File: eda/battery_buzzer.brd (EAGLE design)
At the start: 47 x 26.7 mm, 28 parts, among them Q2 IRFML8244, U1 ISL83491SOIC, U2 ATTINY1634

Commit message: Much tidying in pie.lbr
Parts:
- U2: device pie:SOIC20S -> pie:SOIC20
- moved U2 7.41 mm to (16.5, 14.0), turned to 180 degrees

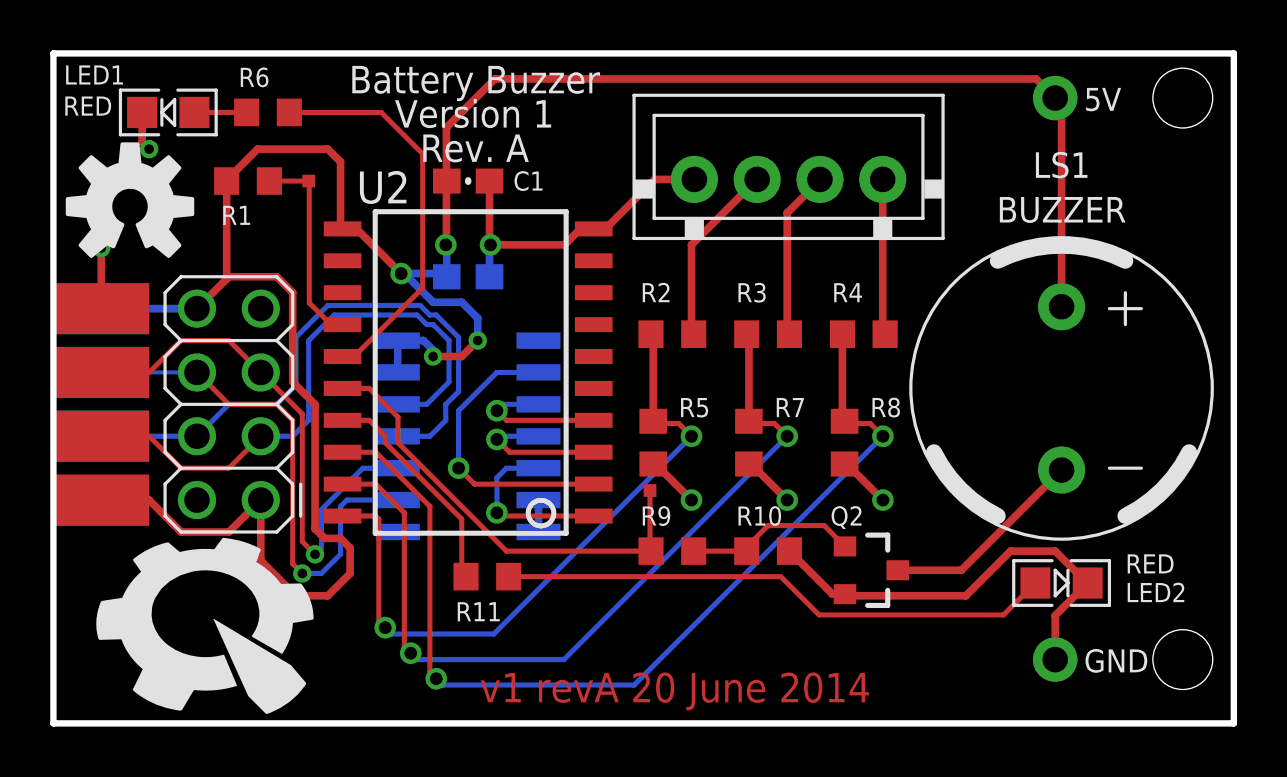
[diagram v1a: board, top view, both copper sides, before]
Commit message: Fixed ribboncable pinout
On battery_buzzer, smartsensor, smartsensor_Powered, team_flag, controller,
and grizzly_bear.
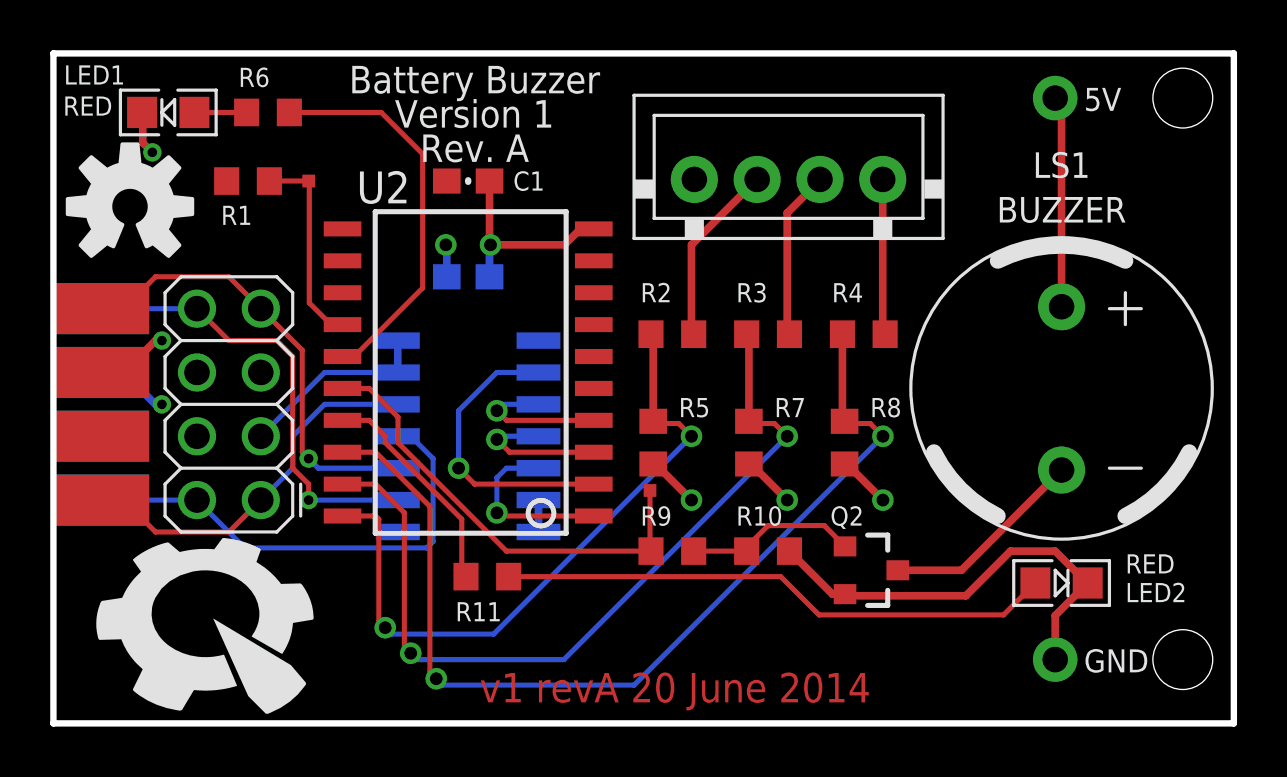
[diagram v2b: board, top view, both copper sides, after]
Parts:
- renumbered U$7 to U$14, U$8 to U$15
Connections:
- net 5V: now also U$14.3, U$14.6, U$15.3, U$15.6; no longer U$14.1, U$14.8, U$15.1, U$15.8
- net A_N: now also U$14.2, U$15.2; no longer U$14.4, U$15.4
- net A_P: now also U$14.1, U$15.1; no longer U$14.3, U$15.3
- net B_N: now also U$14.7, U$15.7; no longer U$14.5, U$15.5
- net B_P: now also U$14.8, U$15.8; no longer U$14.6, U$15.6
- net GND: now also U$14.4, U$14.5, U$15.4, U$15.5; no longer U$14.2, U$14.7, U$15.2, U$15.7
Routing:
- net 5V: track 102.0 -> 21.6 mm, vias 4 -> 2
- net A_P: track 23.2 -> 15.2 mm
- net GND: track 45.3 -> 39.2 mm
- net A_N: track 23.7 -> 19.2 mm
- net B_N: track 21.1 -> 17.9 mm
- net B_P: track 20.8 -> 17.9 mm
- added copper zone on layer 1, net 5V
- removed copper zone on layer 1, net N$8

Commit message: All jigs probe vias accessible after populating.
Also changed "VCC" signal name on jigs to "5V" to match boards.
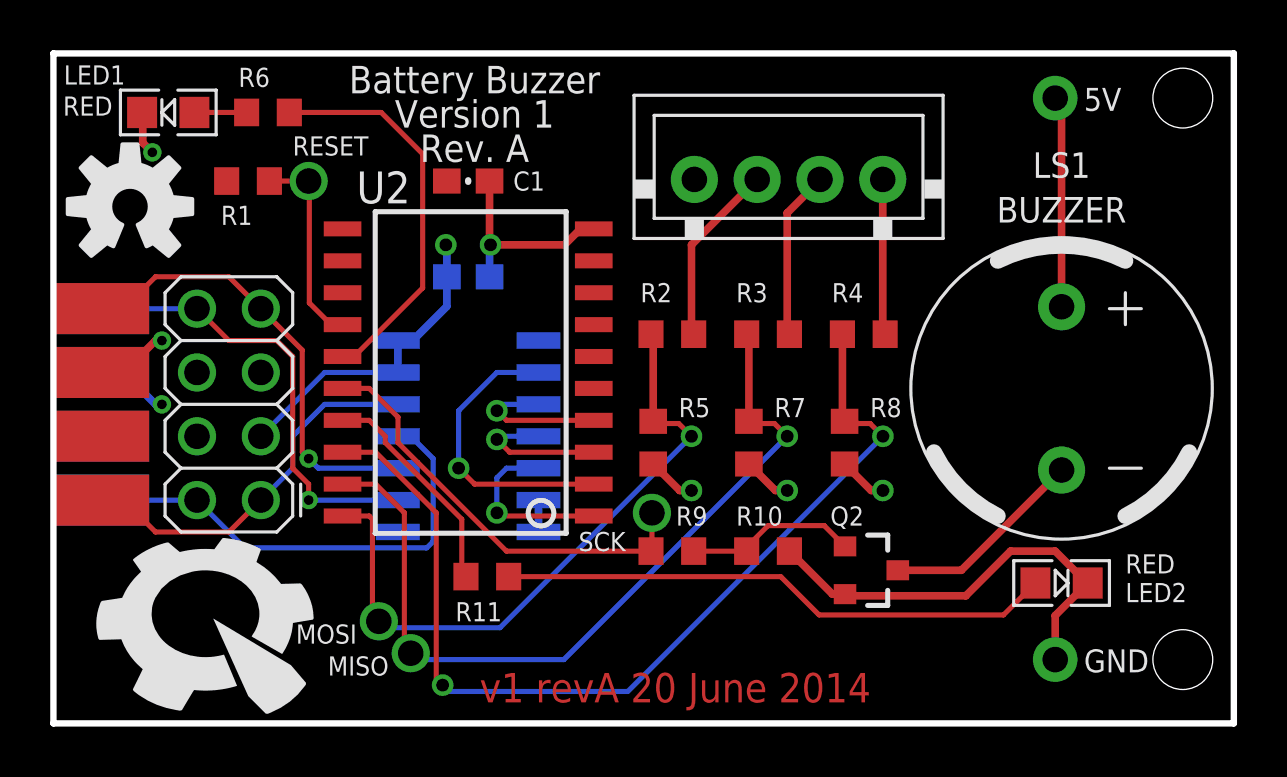
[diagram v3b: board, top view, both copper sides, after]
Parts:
- removed TP1, TP2: TEST-POINT2, pie:PAD.02X.02
- added MISO, MOSI, RESET, SCK: (no value), pie:POGO_PIN_394
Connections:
- net IO1: now also MOSI.POGO_PIN
- net IO2: now also MISO.POGO_PIN
- net IO3: now also SCK.POGO_PIN; no longer TP2.P$1
- net RESET: now also RESET.POGO_PIN; no longer TP1.P$1
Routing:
- net 5V: track 21.6 -> 25.3 mm
- net GND: track 39.2 -> 40.2 mm
- net IO3: track 18.1 -> 17.2 mm
- net IO1: track 26.9 -> 26.6 mm, vias 2 -> 1
- net IO2: vias 2 -> 1

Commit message: battery_buzzer.brd LED orientation and silkscreen fixed.
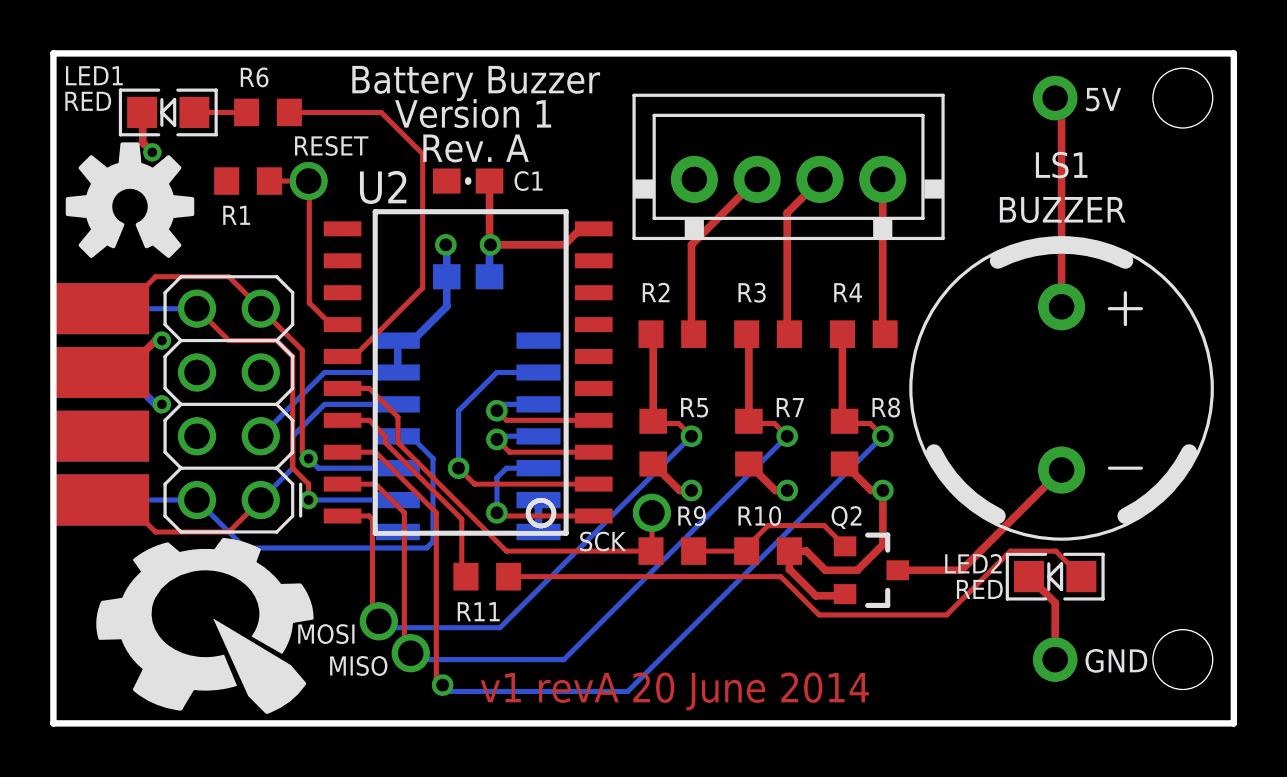
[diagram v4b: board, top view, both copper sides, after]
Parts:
- moved LED2 0.36 mm to (39.9, 5.84), turned to 180 degrees
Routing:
- net GND: track 40.2 -> 36.6 mm
- net N$7: track 22.1 -> 24.9 mm
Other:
- board text added: "10k"
- board text removed: "110k"
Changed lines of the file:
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@@
 <wire x1="0" y1="26.67" x2="0" y2="0" width="0.254" layer="20"/>
 <text x="16.9672" y="0.8382" size="1.1684" layer="1" font="vector" ratio="15">v1 revA 20 June 2014</text>
-<text x="38.354" y="1.016" size="0.762" layer="22" font="vector" ratio="20" rot="MR0">(c) Pioneers in Engineering
+<text x="38.608" y="1.27" size="0.762" layer="22" font="vector" ratio="20" rot="MR0">(c) Pioneers in Engineering
 Design by:
 Vincent Donato, Devin He, and Krystyn Neisess
@@
 Rev. A</text>
 <text x="7.366" y="23.368" size="0.762" layer="27" font="vector" ratio="20" align="top-left">130</text>
-<text x="6.6802" y="19.7104" size="0.762" layer="27" font="vector" ratio="20" align="top-left">110k</text>
+<text x="6.6802" y="19.5834" size="0.762" layer="27" font="vector" ratio="20" align="top-left">10k</text>
 </plain>
 <attributes>
@@
 <element name="LED1" library="pie" package="LED-0805" value="RED" x="4.572" y="24.3205" smashed="yes" rot="R180">
 <attribute name="PIE-INT-REF-NUM" value="LED" x="4.572" y="24.3205" size="1.778" layer="27" rot="R180" display="off"/>
-<attribute name="NAME" x="0.41275" y="25.43175" size="0.762" layer="25" font="vector" ratio="20"/>
-<attribute name="VALUE" x="0.381" y="24.1935" size="0.762" layer="25" font="vector" ratio="20"/>
+<attribute name="NAME" x="0.4064" y="25.4" size="0.762" layer="25" font="vector" ratio="20"/>
+<attribute name="VALUE" x="0.381" y="24.384" size="0.762" layer="25" font="vector" ratio="20"/>
 </element>
 <element name="U$11" library="pie" package="XH_CONNECTOR_4POS_2.5MM" value="XH_CONNECTOR_4POS" x="29.464" y="21.844" smashed="yes">
@@
 <attribute name="VALUE" x="16.002" y="2.921" size="0.762" layer="27" font="vector" ratio="20"/>
 </element>
-<element name="LED2" library="pie" package="LED-0805" value="RED" x="40.132" y="5.588" smashed="yes">
-<attribute name="PIE-INT-REF-NUM" value="LED" x="40.132" y="5.588" size="1.778" layer="27" display="off"/>
-<attribute name="NAME" x="42.672" y="4.826" size="0.762" layer="25" font="vector" ratio="20"/>
-<attribute name="VALUE" x="42.672" y="5.969" size="0.762" layer="25" font="vector" ratio="20"/>
+<element name="LED2" library="pie" package="LED-0805" value="RED" x="39.878" y="5.842" smashed="yes" rot="R180">
+<attribute name="PIE-INT-REF-NUM" value="LED" x="39.878" y="5.842" size="1.778" layer="27" rot="R180" display="off"/>
+<attribute name="NAME" x="37.846" y="6.731" size="0.762" layer="25" font="vector" ratio="20" rot="R180"/>
+<attribute name="VALUE" x="37.846" y="5.715" size="0.762" layer="25" font="vector" ratio="20" rot="R180"/>
 </element>
 <element name="Q2" library="pie" package="SOT23-3" value="IRFML8244" x="32.512" y="6.096" smashed="yes" rot="R270">
@@
 <contactref element="Q2" pad="2"/>
 <contactref element="R10" pad="1"/>
-<wire x1="31.512" y1="5.146" x2="31.01" y2="5.146" width="0.3048" layer="1"/>
-<wire x1="31.01" y1="5.146" x2="29.298" y2="6.858" width="0.3048" layer="1"/>
-<wire x1="41.1734" y1="5.588" x2="41.148" y2="5.588" width="0.3048" layer="1"/>
-<wire x1="41.148" y1="5.588" x2="39.878" y2="6.858" width="0.3048" layer="1"/>
-<wire x1="39.878" y1="6.858" x2="38.1" y2="6.858" width="0.3048" layer="1"/>
-<wire x1="38.1" y1="6.858" x2="36.322" y2="5.08" width="0.3048" layer="1"/>
-<wire x1="36.322" y1="5.08" x2="31.578" y2="5.08" width="0.3048" layer="1"/>
 <wire x1="31.578" y1="5.08" x2="31.512" y2="5.146" width="0.3048" layer="1"/>
-<wire x1="39.878" y1="2.54" x2="39.878" y2="4.2926" width="0.3048" layer="1"/>
-<wire x1="39.878" y1="4.2926" x2="41.1734" y2="5.588" width="0.3048" layer="1"/>
 <via x="29.21" y="9.271" extent="1-16" drill="0.508"/>
 <via x="25.4" y="9.271" extent="1-16" drill="0.508"/>
@@
 <wire x1="33.02" y1="9.271" x2="32.551" y2="9.271" width="0.3048" layer="1"/>
 <wire x1="32.551" y1="9.271" x2="31.496" y2="10.326" width="0.3048" layer="1"/>
+<wire x1="39.878" y1="2.54" x2="39.878" y2="4.8006" width="0.3048" layer="1"/>
+<wire x1="39.878" y1="4.8006" x2="38.8366" y2="5.842" width="0.3048" layer="1"/>
+<wire x1="29.298" y1="6.858" x2="29.298" y2="6.135" width="0.3048" layer="1"/>
+<wire x1="29.298" y1="6.135" x2="30.353" y2="5.08" width="0.3048" layer="1"/>
+<wire x1="30.353" y1="5.08" x2="31.446" y2="5.08" width="0.3048" layer="1"/>
+<wire x1="31.446" y1="5.08" x2="31.512" y2="5.146" width="0.3048" layer="1"/>
+<wire x1="29.298" y1="6.858" x2="29.972" y2="6.858" width="0.3048" layer="1"/>
+<wire x1="29.972" y1="6.858" x2="30.734" y2="6.096" width="0.3048" layer="1"/>
+<wire x1="30.734" y1="6.096" x2="32.004" y2="6.096" width="0.3048" layer="1"/>
+<wire x1="32.004" y1="6.096" x2="33.02" y2="7.112" width="0.3048" layer="1"/>
+<wire x1="33.02" y1="7.112" x2="33.02" y2="9.271" width="0.3048" layer="1"/>
 </signal>
 <signal name="TX">
@@
 <wire x1="18.122" y1="5.842" x2="28.956" y2="5.842" width="0.2032" layer="1"/>
 <wire x1="28.956" y1="5.842" x2="30.48" y2="4.318" width="0.2032" layer="1"/>
-<wire x1="30.48" y1="4.318" x2="37.8206" y2="4.318" width="0.2032" layer="1"/>
-<wire x1="37.8206" y1="4.318" x2="39.0906" y2="5.588" width="0.2032" layer="1"/>
+<wire x1="30.48" y1="4.318" x2="35.56" y2="4.318" width="0.2032" layer="1"/>
+<wire x1="35.56" y1="4.318" x2="38.1" y2="6.858" width="0.2032" layer="1"/>
+<wire x1="38.1" y1="6.858" x2="39.9034" y2="6.858" width="0.2032" layer="1"/>
+<wire x1="39.9034" y1="6.858" x2="40.9194" y2="5.842" width="0.2032" layer="1"/>
 </signal>
 <signal name="LED_BUZZER">

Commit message: Standardized copyright and "Design by" info among boards.
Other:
- board text added: "(c) Pioneers in Engineering. Design by: Vincent Donato, Devin He, and Krystyn Neisess. This design is open source hardware. For more information, visit pioneers.berkeley.edu/opensource."
- board text removed: "(c) Pioneers in Engineering Design by: Vincent Donato, Devin He, and Krystyn Neisess This design is open source hardware. For more information, visit pioneers.berkeley.edu/opensource"
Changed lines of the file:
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@@
 <wire x1="0" y1="26.67" x2="0" y2="0" width="0.254" layer="20"/>
 <text x="16.9672" y="0.8382" size="1.1684" layer="1" font="vector" ratio="15">v1 revA 20 June 2014</text>
-<text x="38.608" y="1.27" size="0.762" layer="22" font="vector" ratio="20" rot="MR0">(c) Pioneers in Engineering
-Design by:
-Vincent Donato, Devin He, and Krystyn Neisess
+<text x="38.227" y="1.397" size="0.762" layer="22" font="vector" ratio="20" rot="MR0">(c) Pioneers in Engineering.
+Design by:  Vincent Donato, Devin He, and Krystyn Neisess.
 This design is open source hardware.
 For more information, visit
-pioneers.berkeley.edu/opensource</text>
+pioneers.berkeley.edu/opensource.</text>
 <text x="16.764" y="22.352" size="1.0922" layer="21" font="vector" ratio="15" distance="25" align="bottom-center">Battery Buzzer
 Version 1
